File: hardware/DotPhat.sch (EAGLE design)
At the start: 57 parts, among them CN1 1X4-BIG, IC1 CAT24M010TS, IC3 SI1145, J3 USB-MICROB, Q1 BSH103, U1 ATMEGA328P-MU-QFN32, U2 TMP102, U3 ATSHA204-TSU, X2 MC-RTC-RV-4162-C7-I2C, X3 S4B-ZR

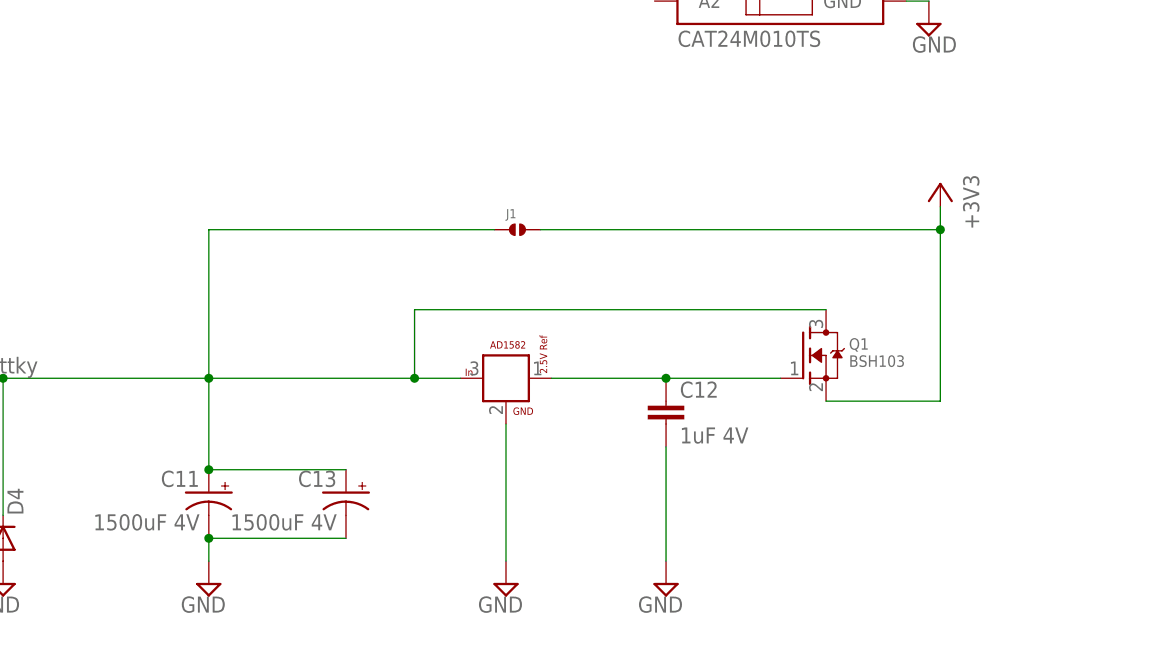
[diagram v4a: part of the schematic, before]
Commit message: Add 3rd solar cap
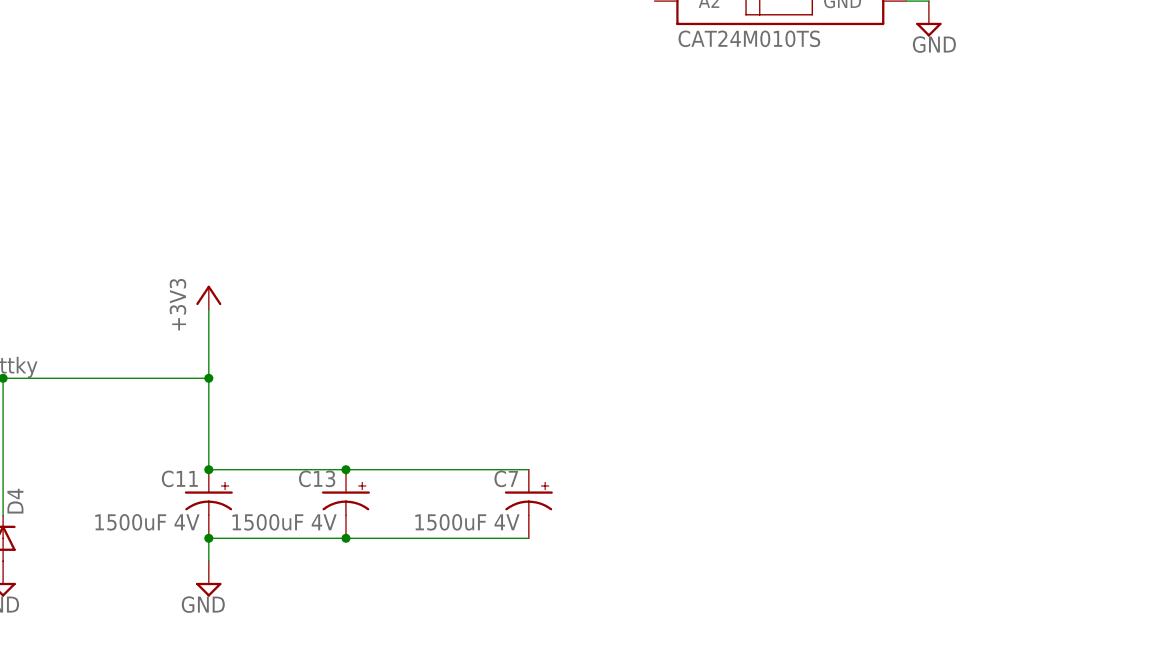
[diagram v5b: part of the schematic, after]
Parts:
- removed C12: 1uF 4V, rcl:C-EUC0603
- removed J1: (no value), solderjumper:SOLDERJUMPER.2.MED
- removed Q1: BSH103, adafruit:MOSFET-NREFLOW
- removed U$4: AD1582, AD1582:AD1582
- added C7: 1500uF 4V, adafruit:CPOL-USCT7343
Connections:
- removed net CAPS_VCC: C11.+, C13.+, D4.C, D5.C, J1.1, Q1.D, U$4.P$3
- removed net MOSFET: C12.1, Q1.G, U$4.P$1
- net +3V3: now also C11.+, C13.+, C7.+, D4.C, D5.C; no longer J1.2, Q1.S
- net GND: now also C7.-; no longer C12.2, U$4.P$2
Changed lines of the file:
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@@
 <part name="C13" library="adafruit" deviceset="CPOL-US" device="CT7343" value="1500uF 4V"/>
 <part name="SUPPLY34" library="supply2" deviceset="GND" device=""/>
-<part name="+3V22" library="supply1" deviceset="+3V3" device=""/>
-<part name="SUPPLY36" library="supply2" deviceset="GND" device=""/>
 <part name="D5" library="diode" deviceset="DIODE-" device="SOD523" value="0.3V Schottky"/>
-<part name="Q1" library="adafruit" deviceset="MOSFET-N" device="REFLOW" value="BSH103"/>
-<part name="U$4" library="AD1582" deviceset="AD1582" device=""/>
-<part name="SUPPLY19" library="supply2" deviceset="GND" device=""/>
-<part name="C12" library="rcl" deviceset="C-EU" device="C0603" value="1uF 4V"/>
 <part name="IC3" library="silabs" deviceset="SI114*" device="" technology="5"/>
 <part name="SUPPLY37" library="supply2" deviceset="GND" device=""/>
 <part name="+3V23" library="supply1" deviceset="+3V3" device=""/>
 <part name="TP1" library="SparkFun" deviceset="TEST-POINT" device="3"/>
-<part name="J1" library="solderjumper" deviceset="SOLDERJUMPER.2" device=".MED"/>
+<part name="C7" library="adafruit" deviceset="CPOL-US" device="CT7343" value="1500uF 4V"/>
+<part name="+3V3" library="supply1" deviceset="+3V3" device=""/>
 </parts>
 <sheets>
@@
 <instance part="C13" gate="G$1" x="46.99" y="-222.25" rot="MR0"/>
 <instance part="SUPPLY34" gate="GND" x="8.89" y="-232.41" rot="MR0"/>
-<instance part="+3V22" gate="G$1" x="113.03" y="-187.96" rot="MR0"/>
-<instance part="SUPPLY36" gate="GND" x="82.55" y="-232.41" rot="MR0"/>
 <instance part="D5" gate="G$1" x="-5.08" y="-209.55" rot="MR180"/>
-<instance part="Q1" gate="G$1" x="97.79" y="-207.01"/>
-<instance part="U$4" gate="G$1" x="64.77" y="-212.09"/>
-<instance part="SUPPLY19" gate="GND" x="64.77" y="-232.41" rot="MR0"/>
-<instance part="C12" gate="G$1" x="82.55" y="-212.09"/>
 <instance part="IC3" gate="G$1" x="180.34" y="-215.9"/>
 <instance part="SUPPLY37" gate="GND" x="170.18" y="-228.6" rot="MR0"/>
 <instance part="+3V23" gate="G$1" x="149.86" y="-203.2"/>
 <instance part="TP1" gate="G$1" x="-50.8" y="68.58" rot="R180"/>
-<instance part="J1" gate="G$1" x="66.04" y="-193.04"/>
+<instance part="C7" gate="G$1" x="67.31" y="-222.25" rot="MR0"/>
+<instance part="+3V3" gate="G$1" x="31.75" y="-199.39"/>
 </instances>
 <busses>
@@
 <pinref part="C13" gate="G$1" pin="-"/>
 <wire x1="31.75" y1="-227.33" x2="46.99" y2="-227.33" width="0.1524" layer="91"/>
+<pinref part="C7" gate="G$1" pin="-"/>
+<wire x1="67.31" y1="-227.33" x2="46.99" y2="-227.33" width="0.1524" layer="91"/>
+<junction x="46.99" y="-227.33"/>
 </segment>
 <segment>
 <pinref part="D4" gate="G$1" pin="A"/>
 <pinref part="SUPPLY34" gate="GND" pin="GND"/>
-</segment>
-<segment>
-<pinref part="SUPPLY36" gate="GND" pin="GND"/>
-<pinref part="C12" gate="G$1" pin="2"/>
-<wire x1="82.55" y1="-229.87" x2="82.55" y2="-217.17" width="0.1524" layer="91"/>
-</segment>
-<segment>
-<pinref part="U$4" gate="G$1" pin="P$2"/>
-<pinref part="SUPPLY19" gate="GND" pin="GND"/>
-<wire x1="64.77" y1="-229.87" x2="64.77" y2="-214.63" width="0.1524" layer="91"/>
 </segment>
 <segment>
@@
 </segment>
 <segment>
-<pinref part="+3V22" gate="G$1" pin="+3V3"/>
-<pinref part="Q1" gate="G$1" pin="S"/>
-<wire x1="113.03" y1="-212.09" x2="113.03" y2="-193.04" width="0.1524" layer="91"/>
-<wire x1="113.03" y1="-193.04" x2="113.03" y2="-190.5" width="0.1524" layer="91"/>
-<wire x1="100.33" y1="-212.09" x2="113.03" y2="-212.09" width="0.1524" layer="91"/>
-<pinref part="J1" gate="G$1" pin="2"/>
-<wire x1="68.58" y1="-193.04" x2="113.03" y2="-193.04" width="0.1524" layer="91"/>
-<junction x="113.03" y="-193.04"/>
-</segment>
-<segment>
 <pinref part="+3V23" gate="G$1" pin="+3V3"/>
 <wire x1="149.86" y1="-205.74" x2="170.18" y2="-205.74" width="0.1524" layer="91"/>
 <pinref part="IC3" gate="G$1" pin="VDD"/>
+</segment>
+<segment>
+<pinref part="C13" gate="G$1" pin="+"/>
+<pinref part="C11" gate="G$1" pin="+"/>
+<wire x1="46.99" y1="-219.71" x2="31.75" y2="-219.71" width="0.1524" layer="91"/>
+<junction x="31.75" y="-219.71"/>
+<wire x1="31.75" y1="-209.55" x2="31.75" y2="-219.71" width="0.1524" layer="91"/>
+<pinref part="D5" gate="G$1" pin="C"/>
+<wire x1="-2.54" y1="-209.55" x2="8.89" y2="-209.55" width="0.1524" layer="91"/>
+<wire x1="8.89" y1="-209.55" x2="31.75" y2="-209.55" width="0.1524" layer="91"/>
+<pinref part="D4" gate="G$1" pin="C"/>
+<wire x1="8.89" y1="-224.79" x2="8.89" y2="-209.55" width="0.1524" layer="91"/>
+<junction x="8.89" y="-209.55"/>
+<pinref part="C7" gate="G$1" pin="+"/>
+<wire x1="67.31" y1="-219.71" x2="46.99" y2="-219.71" width="0.1524" layer="91"/>
+<junction x="46.99" y="-219.71"/>
+<pinref part="+3V3" gate="G$1" pin="+3V3"/>
+<wire x1="31.75" y1="-201.93" x2="31.75" y2="-209.55" width="0.1524" layer="91"/>
+<junction x="31.75" y="-209.55"/>
 </segment>
 </net>
@@
 </segment>
 </net>
-<net name="CAPS_VCC" class="0">
-<segment>
-<pinref part="C13" gate="G$1" pin="+"/>
-<pinref part="C11" gate="G$1" pin="+"/>
-<wire x1="46.99" y1="-219.71" x2="31.75" y2="-219.71" width="0.1524" layer="91"/>
-<junction x="31.75" y="-219.71"/>
-<pinref part="U$4" gate="G$1" pin="P$3"/>
-<wire x1="59.69" y1="-209.55" x2="54.61" y2="-209.55" width="0.1524" layer="91"/>
-<wire x1="54.61" y1="-209.55" x2="31.75" y2="-209.55" width="0.1524" layer="91"/>
-<wire x1="31.75" y1="-209.55" x2="31.75" y2="-219.71" width="0.1524" layer="91"/>
-<pinref part="D5" gate="G$1" pin="C"/>
-<wire x1="-2.54" y1="-209.55" x2="8.89" y2="-209.55" width="0.1524" layer="91"/>
-<junction x="31.75" y="-209.55"/>
-<wire x1="8.89" y1="-209.55" x2="31.75" y2="-209.55" width="0.1524" layer="91"/>
-<pinref part="D4" gate="G$1" pin="C"/>
-<wire x1="8.89" y1="-224.79" x2="8.89" y2="-209.55" width="0.1524" layer="91"/>
-<junction x="8.89" y="-209.55"/>
-<pinref part="Q1" gate="G$1" pin="D"/>
-<wire x1="100.33" y1="-201.93" x2="54.61" y2="-201.93" width="0.1524" layer="91"/>
-<wire x1="54.61" y1="-201.93" x2="54.61" y2="-209.55" width="0.1524" layer="91"/>
-<junction x="54.61" y="-209.55"/>
-<pinref part="J1" gate="G$1" pin="1"/>
-<wire x1="63.5" y1="-193.04" x2="31.75" y2="-193.04" width="0.1524" layer="91"/>
-<wire x1="31.75" y1="-193.04" x2="31.75" y2="-209.55" width="0.1524" layer="91"/>
-</segment>
-</net>
-<net name="MOSFET" class="0">
-<segment>
-<pinref part="Q1" gate="G$1" pin="G"/>
-<wire x1="95.25" y1="-209.55" x2="82.55" y2="-209.55" width="0.1524" layer="91"/>
-<pinref part="U$4" gate="G$1" pin="P$1"/>
-<wire x1="82.55" y1="-209.55" x2="69.85" y2="-209.55" width="0.1524" layer="91"/>
-<pinref part="C12" gate="G$1" pin="1"/>
-<junction x="82.55" y="-209.55"/>
-</segment>
-</net>

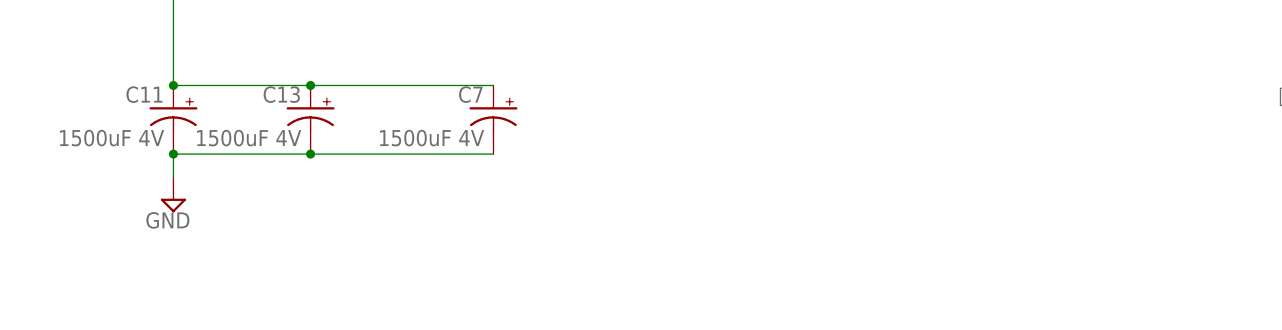
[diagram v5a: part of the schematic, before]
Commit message: Add capacity buget calculation
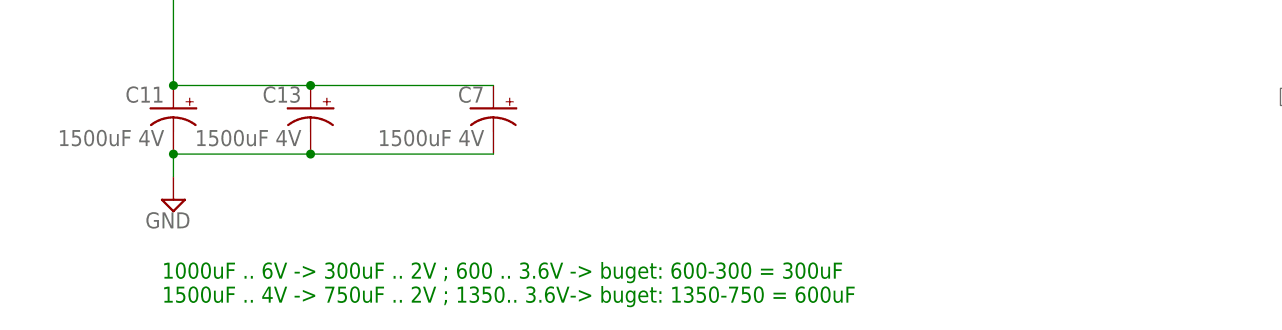
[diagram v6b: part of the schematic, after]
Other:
- note added: "1000uF .. 6V -> 300uF .. 2V ; 600 .. 3.6V -> buget: 600-300 = 300uF 1500uF .. 4V -> 750uF .. 2V ; 1350.. 3.6V-> buget: 1350-750 = 600uF"
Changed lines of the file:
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@@
 <text x="-48.26" y="38.1" size="1.27" layer="91">Radio Tx
 -Cyan-</text>
+<text x="30.48" y="-243.84" size="1.778" layer="91">1000uF .. 6V -&gt; 300uF .. 2V ; 600 .. 3.6V -&gt; buget: 600-300 = 300uF
+1500uF .. 4V -&gt; 750uF .. 2V ; 1350.. 3.6V-&gt; buget: 1350-750 = 600uF</text>
 </plain>
 <instances>
